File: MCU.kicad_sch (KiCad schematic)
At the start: 0 parts

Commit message: MCU schematic
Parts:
- added C10, C11, C12, C5, C6, C7, C8, C9: 0.1uF, symbol Device:C
- added C4: 10uF, symbol Device:C
- added R3: 10k, symbol Device:R
- added S1, S2: TS04-66-65-BK-100-SMT, TS04-66-65-BK-100-SMT:SW_TS04-66-65-BK-100-SMT, symbol KeyboardSymbols:TS04-66-65-BK-100-SMT
- added TP1: 3.3V, symbol Connector:TestPoint
- added TP2: SWDIO, symbol Connector:TestPoint
- added TP3: SWCLK, symbol Connector:TestPoint
- added TP4: GND, symbol Connector:TestPoint
- added TP5: NRST, symbol Connector:TestPoint
- added U3: STM32F072CBTx, Package_QFP:LQFP-48_7x7mm_P0.5mm, symbol MCU_ST_STM32F0:STM32F072CBTx
- added U4: AT24C32E-SSHM-T, 8S1_MCH, symbol KeyboardSymbols:AT24C32E-SSHM-T
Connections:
- new net +3.3V: C12.1, C4.1, C5.1, C6.1, C7.1, C8.1, C9.1, S2.1, S2.3, TP1.1, U3.1 (VBAT), U3.24 (VDD), U3.36 (VDDIO2), U3.48 (VDD), U3.9 (VDDA), U4.8 (VCC)
- new net BOOT: C11.1, R3.1, S2.2, S2.4, U3.44 (BOOT0)
- new net COL0: U3.10 (PA0)
- new net COL1: U3.11 (PA1)
- new net COL10: U3.31 (PA10)
- new net COL11: U3.26 (PB13)
- new net COL12: U3.27 (PB14)
- new net COL13: U3.28 (PB15)
- new net COL14: U3.2 (PC13)
- new net COL2: U3.12 (PA2)
- new net COL3: U3.13 (PA3)
- new net COL4: U3.14 (PA4)
- new net COL5: U3.15 (PA5)
- new net COL6: U3.16 (PA6)
- new net COL7: U3.17 (PA7)
- new net COL8: U3.29 (PA8)
- new net COL9: U3.30 (PA9)
- new net EEPROM_SCL: U3.42 (PB6), U4.6 (SCL)
- new net EEPROM_SDA: U3.43 (PB7), U4.5 (SDA)
- new net GND: C10.2, C11.2, C12.2, C4.2, C5.2, C6.2, C7.2, C8.2, C9.2, R3.2, S1.2, S1.4, TP4.1, U3.23 (VSS), U3.35 (VSS), U3.47 (VSS), U3.8 (VSSA), U4.1 (A0), U4.2 (A1), U4.3 (A2), U4.4 (GND), U4.7 (WP)
- new net LED_DATA: U3.38 (PA15)
- new net NRST: C10.1, S1.1, S1.3, TP5.1, U3.7 (NRST)
- new net ROW0: U3.18 (PB0)
- new net ROW1: U3.19 (PB1)
- new net ROW2: U3.20 (PB2)
- new net ROW3: U3.21 (PB10)
- new net SWCLK: TP3.1, U3.37 (PA14)
- new net SWDIO: TP2.1, U3.34 (PA13)
- new net USB_D_N: U3.32 (PA11)
- new net USB_D_P: U3.33 (PA12)

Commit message: peripherals finished
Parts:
- removed C12: 0.1uF, symbol Device:C
- removed U4: AT24C32E-SSHM-T, 8S1_MCH, symbol KeyboardSymbols:AT24C32E-SSHM-T
- added R4, R5: 4.7k, symbol Device:R
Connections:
- net +3.3V: now also R4.1, R5.1
- net COL10: now also U3.27 (PB14); no longer U3.31 (PA10)
- net COL11: now also U3.28 (PB15); no longer U3.26 (PB13)
- net COL12: now also U3.2 (PC13); no longer U3.27 (PB14)
- net COL13: now also U3.5 (PF0); no longer U3.28 (PB15)
- net COL14: now also U3.6 (PF1); no longer U3.2 (PC13)
- net COL4: now also U3.29 (PA8); no longer U3.14 (PA4)
- net COL5: now also U3.30 (PA9); no longer U3.15 (PA5)
- net COL6: now also U3.31 (PA10); no longer U3.16 (PA6)
- net COL7: now also U3.45 (PB8); no longer U3.17 (PA7)
- net COL8: now also U3.46 (PB9); no longer U3.29 (PA8)
- net COL9: now also U3.26 (PB13); no longer U3.30 (PA9)
- net EEPROM_SCL: now also R4.2
- net EEPROM_SDA: now also R5.2
- net ENC_A: now reaches U3.39 (PB3)
- net ENC_B: now reaches U3.40 (PB4)
- net ENC_SW: now reaches U3.41 (PB5)
- new net SCREEN_CS: U3.14 (PA4)
- new net SCREEN_DS: U3.16 (PA6)
- new net SCREEN_SCL: U3.15 (PA5)
- new net SCREEN_SDA: U3.17 (PA7)
- no-connect marks 0 -> 2

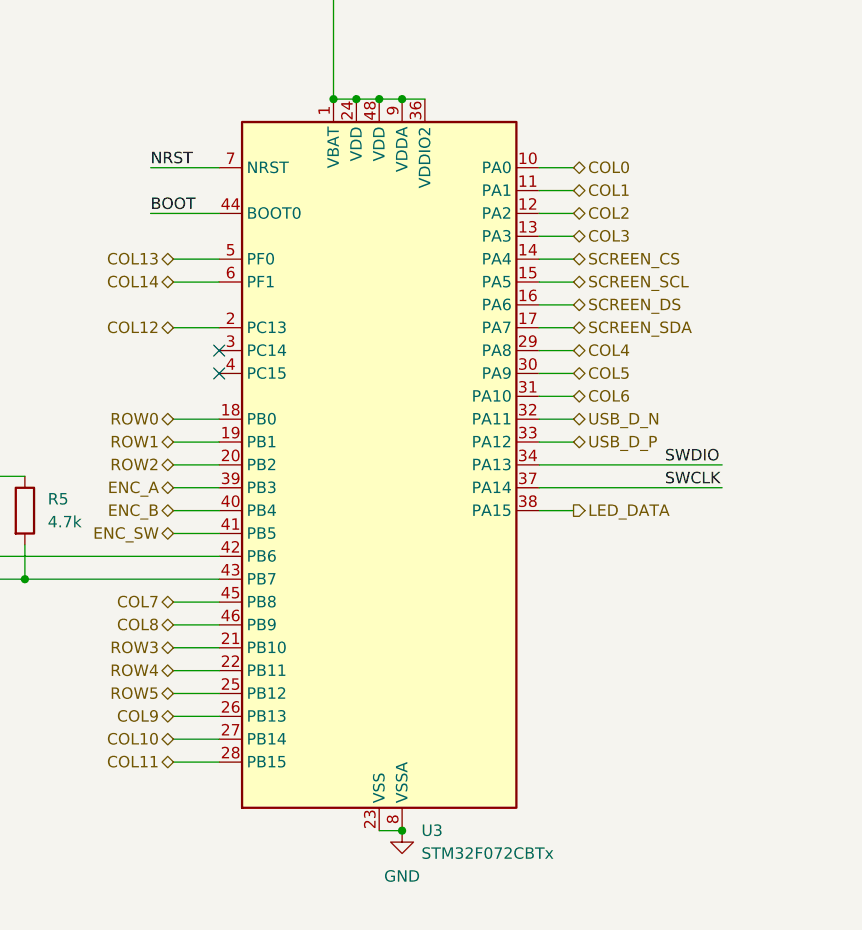
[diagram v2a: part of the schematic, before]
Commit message: switch matrix set-up
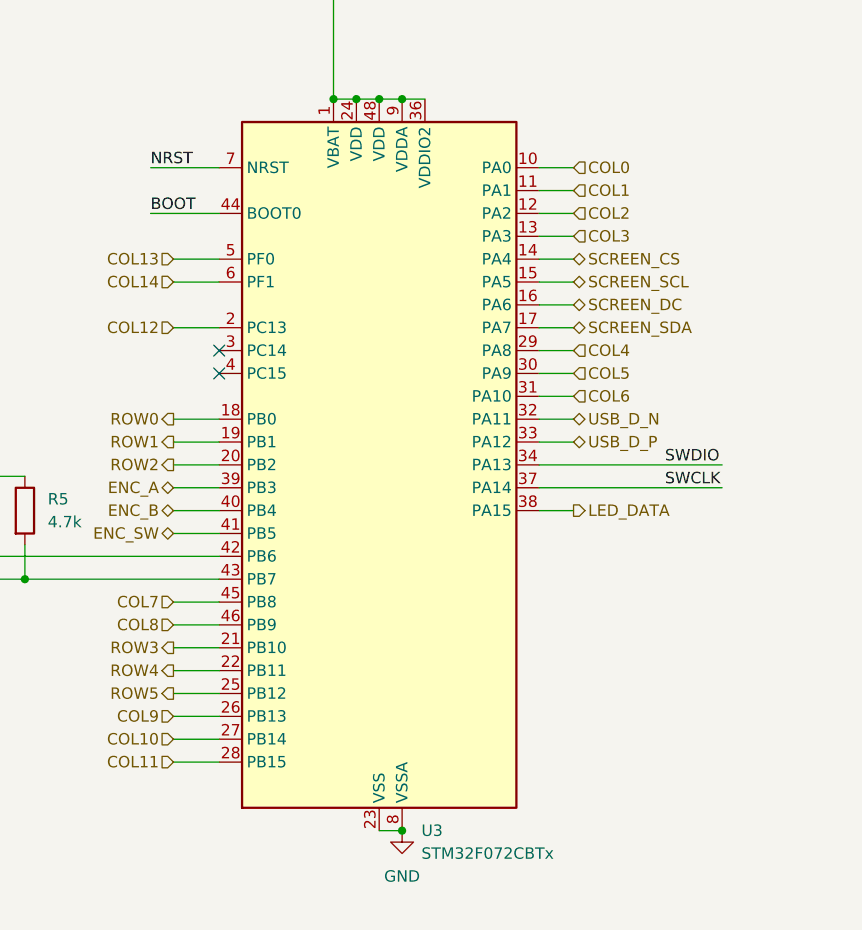
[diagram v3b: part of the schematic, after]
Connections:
- net SCREEN_DS renamed SCREEN_DC
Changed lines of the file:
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@@
 	)
 	(hierarchical_label "COL10"
-		(shape bidirectional)
+		(shape input)
 		(at 124.46 115.57 180)
 		(effects
@@
 	)
 	(hierarchical_label "COL12"
-		(shape bidirectional)
+		(shape input)
 		(at 124.46 69.85 180)
 		(effects
@@
 	)
 	(hierarchical_label "ROW3"
-		(shape bidirectional)
+		(shape output)
 		(at 124.46 105.41 180)
 		(effects
@@
 	)
 	(hierarchical_label "COL4"
-		(shape bidirectional)
+		(shape input)
 		(at 168.91 72.39 0)
 		(effects
@@
 	)
 	(hierarchical_label "ROW2"
-		(shape bidirectional)
+		(shape output)
 		(at 124.46 85.09 180)
 		(effects
@@
 	)
 	(hierarchical_label "COL8"
-		(shape bidirectional)
+		(shape input)
 		(at 124.46 102.87 180)
 		(effects
@@
 	)
 	(hierarchical_label "COL13"
-		(shape bidirectional)
+		(shape input)
 		(at 124.46 62.23 180)
 		(effects
@@
 	)
 	(hierarchical_label "COL9"
-		(shape bidirectional)
+		(shape input)
 		(at 124.46 113.03 180)
 		(effects
@@
 	)
 	(hierarchical_label "COL3"
-		(shape bidirectional)
+		(shape input)
 		(at 168.91 59.69 0)
 		(effects
@@
 	)
 	(hierarchical_label "COL1"
-		(shape bidirectional)
+		(shape input)
 		(at 168.91 54.61 0)
 		(effects
@@
 	)
 	(hierarchical_label "COL5"
-		(shape bidirectional)
+		(shape input)
 		(at 168.91 74.93 0)
 		(effects
@@
 	)
 	(hierarchical_label "ROW1"
-		(shape bidirectional)
+		(shape output)
 		(at 124.46 82.55 180)
 		(effects
@@
 	)
 	(hierarchical_label "ROW4"
-		(shape bidirectional)
+		(shape output)
 		(at 124.4532 107.9552 180)
 		(effects
@@
 	)
 	(hierarchical_label "COL11"
-		(shape bidirectional)
+		(shape input)
 		(at 124.46 118.11 180)
 		(effects
@@
 	)
 	(hierarchical_label "COL14"
-		(shape bidirectional)
+		(shape input)
 		(at 124.46 64.77 180)
 		(effects
@@
 	)
 	(hierarchical_label "COL2"
-		(shape bidirectional)
+		(shape input)
 		(at 168.91 57.15 0)
 		(effects
@@
 	)
 	(hierarchical_label "COL7"
-		(shape bidirectional)
+		(shape input)
 		(at 124.46 100.33 180)
 		(effects
@@
 	)
 	(hierarchical_label "ROW0"
-		(shape bidirectional)
+		(shape output)
 		(at 124.46 80.01 180)
 		(effects
@@
 		)
 	)
-	(hierarchical_label "SCREEN_DS"
+	(hierarchical_label "SCREEN_DC"
 		(shape bidirectional)
 		(at 168.91 67.31 0)
@@
 	)
 	(hierarchical_label "ROW5"
-		(shape bidirectional)
+		(shape output)
 		(at 124.4532 110.4952 180)
 		(effects
@@
 	)
 	(hierarchical_label "COL6"
-		(shape bidirectional)
+		(shape input)
 		(at 168.91 77.47 0)
 		(effects
@@
 	)
 	(hierarchical_label "COL0"
-		(shape bidirectional)
+		(shape input)
 		(at 168.91 52.07 0)
 		(effects
@@
 		)
 		(instances
-			(project "MCU_and_EEPROM"
+			(project "MCU"
 				(path "/e0c3ce79-4e6b-469a-8326-344d8040e74c"
 					(reference "TP4")
@@
 		)
 		(instances
-			(project "MCU_and_EEPROM"
+			(project "MCU"
 				(path "/e0c3ce79-4e6b-469a-8326-344d8040e74c"
 					(reference "C11")
@@
 		)
 		(instances
-			(project "MCU_and_EEPROM"
+			(project "MCU"
 				(path "/e0c3ce79-4e6b-469a-8326-344d8040e74c"
 					(reference "#PWR012")
@@
 		)
 		(instances
-			(project "MCU_and_EEPROM"
+			(project "MCU"
 				(path "/e0c3ce79-4e6b-469a-8326-344d8040e74c"
 					(reference "#PWR013")
@@
 		)
 		(instances
-			(project "MCU_and_EEPROM"
+			(project "MCU"
 				(path "/e0c3ce79-4e6b-469a-8326-344d8040e74c"
 					(reference "C4")
@@
 		)
 		(instances
-			(project "MCU_and_EEPROM"
+			(project "MCU"
 				(path "/e0c3ce79-4e6b-469a-8326-344d8040e74c"
 					(reference "#PWR018")
@@
 		)
 		(instances
-			(project "MCU_and_EEPROM"
+			(project "MCU"
 				(path "/e0c3ce79-4e6b-469a-8326-344d8040e74c"
 					(reference "TP2")
@@
 		)
 		(instances
-			(project "MCU_and_EEPROM"
+			(project "MCU"
 				(path "/e0c3ce79-4e6b-469a-8326-344d8040e74c"
 					(reference "TP5")
@@
 		)
 		(instances
-			(project "MCU_and_EEPROM"
+			(project "MCU"
 				(path "/e0c3ce79-4e6b-469a-8326-344d8040e74c"
 					(reference "#PWR015")
@@
 		)
 		(instances
-			(project "MCU_and_EEPROM"
+			(project "MCU"
 				(path "/e0c3ce79-4e6b-469a-8326-344d8040e74c"
 					(reference "#PWR011")
@@
 		)
 		(instances
-			(project "MCU_and_EEPROM"
+			(project "MCU"
 				(path "/e0c3ce79-4e6b-469a-8326-344d8040e74c"
 					(reference "C8")
@@
 		)
 		(instances
-			(project "MCU_and_EEPROM"
+			(project "MCU"
 				(path "/e0c3ce79-4e6b-469a-8326-344d8040e74c"
 					(reference "#PWR017")
@@
 		)
 		(instances
-			(project "MCU_and_EEPROM"
+			(project "MCU"
 				(path "/e0c3ce79-4e6b-469a-8326-344d8040e74c"
 					(reference "TP1")
@@
 		)
 		(instances
-			(project "MCU_and_EEPROM"
+			(project "MCU"
 				(path "/e0c3ce79-4e6b-469a-8326-344d8040e74c"
 					(reference "#PWR016")
@@
 		)
 		(instances
-			(project "MCU_and_EEPROM"
+			(project "MCU"
 				(path "/e0c3ce79-4e6b-469a-8326-344d8040e74c"
 					(reference "S1")
@@
 		)
 		(instances
-			(project "MCU_and_EEPROM"
+			(project "MCU"
 				(path "/e0c3ce79-4e6b-469a-8326-344d8040e74c"
 					(reference "TP3")
@@
 		)
 		(instances
-			(project "MCU_and_EEPROM"
+			(project "MCU"
 				(path "/e0c3ce79-4e6b-469a-8326-344d8040e74c"
 					(reference "R3")
@@
 		)
 		(instances
+			(project "MCU"
+				(path "/e0c3ce79-4e6b-469a-8326-344d8040e74c"
+					(reference "#PWR023")
+					(unit 1)
+				)
+			)
 			(project "octo_keyboard"
 				(path "/e2f6b5f5-4c68-42ad-a343-f16c1cb3ab86/675d025f-eeea-4859-baf0-94302a86ce27"
@@
 		)
 		(instances
-			(project "MCU_and_EEPROM"
+			(project "MCU"
 				(path "/e0c3ce79-4e6b-469a-8326-344d8040e74c"
 					(reference "C9")
@@
 		)
 		(instances
-			(project "MCU_and_EEPROM"
+			(project "MCU"
 				(path "/e0c3ce79-4e6b-469a-8326-344d8040e74c"
 					(reference "S2")
@@
 		)
 		(instances
-			(project "MCU_and_EEPROM"
+			(project "MCU"
 				(path "/e0c3ce79-4e6b-469a-8326-344d8040e74c"
 					(reference "#PWR014")
@@
 		)
 		(instances
+			(project "MCU"
+				(path "/e0c3ce79-4e6b-469a-8326-344d8040e74c"
+					(reference "R5")
+					(unit 1)
+				)
+			)
 			(project "octo_keyboard"
 				(path "/e2f6b5f5-4c68-42ad-a343-f16c1cb3ab86/675d025f-eeea-4859-baf0-94302a86ce27"
@@
 		)
 		(instances
+			(project "MCU"
+				(path "/e0c3ce79-4e6b-469a-8326-344d8040e74c"
+					(reference "R4")
+					(unit 1)
+				)
+			)
 			(project "octo_keyboard"
 				(path "/e2f6b5f5-4c68-42ad-a343-f16c1cb3ab86/675d025f-eeea-4859-baf0-94302a86ce27"
@@
 		)
 		(instances
-			(project "MCU_and_EEPROM"
+			(project "MCU"
 				(path "/e0c3ce79-4e6b-469a-8326-344d8040e74c"
 					(reference "C6")
@@
 		)
 		(instances
-			(project "MCU_and_EEPROM"
+			(project "MCU"
 				(path "/e0c3ce79-4e6b-469a-8326-344d8040e74c"
 					(reference "C10")
@@
 		)
 		(instances
-			(project "MCU_and_EEPROM"
+			(project "MCU"
 				(path "/e0c3ce79-4e6b-469a-8326-344d8040e74c"
 					(reference "U3")
@@
 		)
 		(instances
-			(project "MCU_and_EEPROM"
+			(project "MCU"
 				(path "/e0c3ce79-4e6b-469a-8326-344d8040e74c"
 					(reference "C5")
@@
 		)
 		(instances
-			(project "MCU_and_EEPROM"
+			(project "MCU"
 				(path "/e0c3ce79-4e6b-469a-8326-344d8040e74c"
 					(reference "C7")

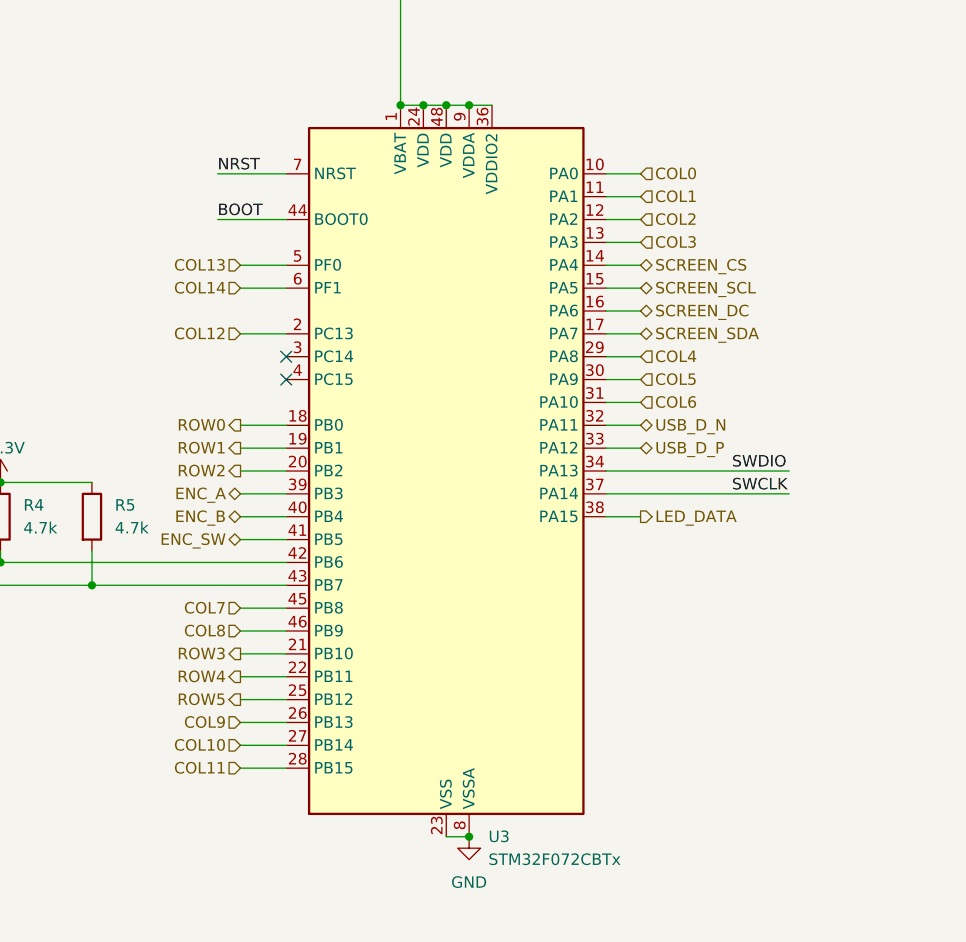
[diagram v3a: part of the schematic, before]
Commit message: cleaned up top-level connections
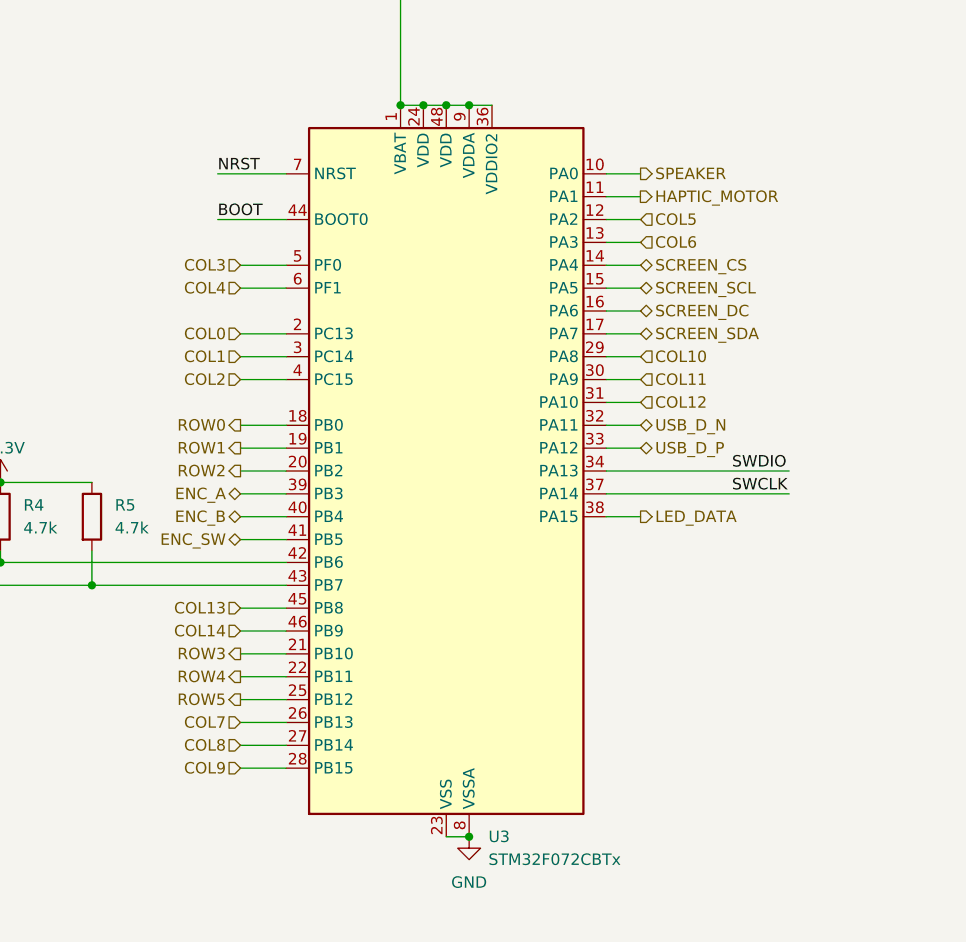
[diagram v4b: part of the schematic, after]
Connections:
- net COL0: now also U3.2 (PC13); no longer U3.10 (PA0)
- net COL1: now also U3.3 (PC14); no longer U3.11 (PA1)
- net COL10: now also U3.29 (PA8); no longer U3.27 (PB14)
- net COL11: now also U3.30 (PA9); no longer U3.28 (PB15)
- net COL12: now also U3.31 (PA10); no longer U3.2 (PC13)
- net COL13: now also U3.45 (PB8); no longer U3.5 (PF0)
- net COL14: now also U3.46 (PB9); no longer U3.6 (PF1)
- net COL2: now also U3.4 (PC15); no longer U3.12 (PA2)
- net COL3: now also U3.5 (PF0); no longer U3.13 (PA3)
- net COL4: now also U3.6 (PF1); no longer U3.29 (PA8)
- net COL5: now also U3.12 (PA2); no longer U3.30 (PA9)
- net COL6: now also U3.13 (PA3); no longer U3.31 (PA10)
- net COL7: now also U3.26 (PB13); no longer U3.45 (PB8)
- net COL8: now also U3.27 (PB14); no longer U3.46 (PB9)
- net COL9: now also U3.28 (PB15); no longer U3.26 (PB13)
- new net HAPTIC_MOTOR: U3.11 (PA1)
- new net SPEAKER: U3.10 (PA0)
- no-connect marks 2 -> 0
